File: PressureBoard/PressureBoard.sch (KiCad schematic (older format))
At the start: 9 parts, among them J1 Jack-DC, U1 MCP6002-xP, U2 L78L05_TO92

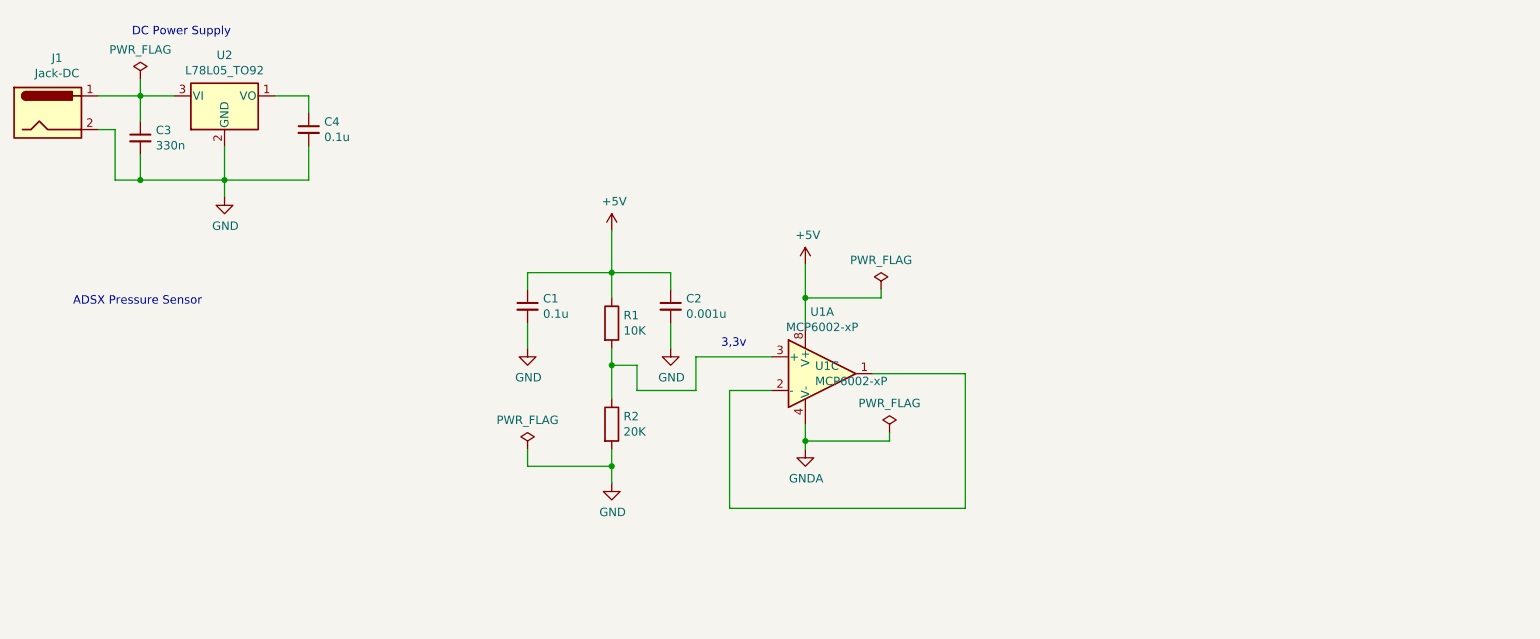
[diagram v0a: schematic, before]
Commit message: Agrego segunda versión del esquemático que incluye regulador LM7805 y sensor ASDX
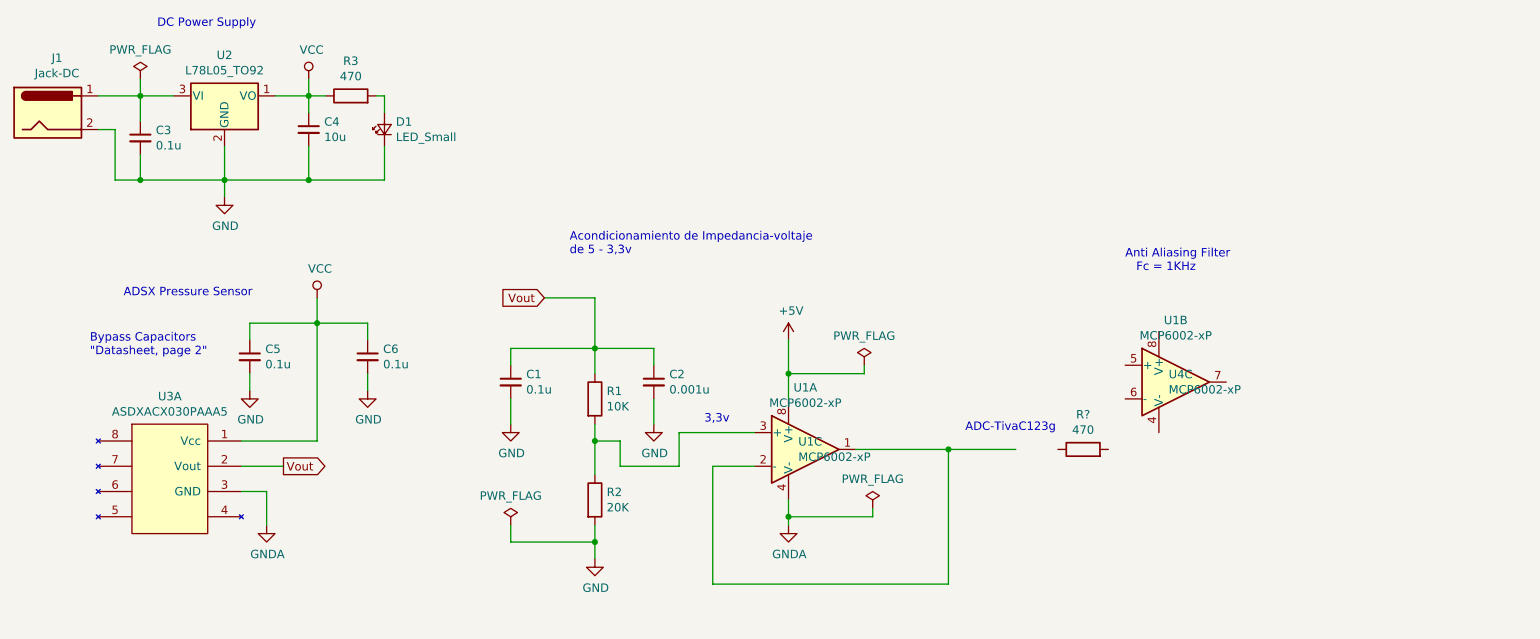
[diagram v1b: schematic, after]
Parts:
- added C5, C6: 0.1u, symbol Device:C_Small
- added D1: LED_Small, symbol Device:LED_Small
- added R3, R?: 470, symbol Device:R
- added unit 2 of U1
- added U3: ASDXACX030PAAA5, symbol ASDX:ASDXACX030PAAA5
- added U4: MCP6002-xP, symbol Amplifier_Operational:MCP6002-xP
- C3: value 330n -> 0.1u
- C4: value 0.1u -> 10u
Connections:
- net +5V: no longer C1.1, C2.1, R1.1
- net GND: now also C5.2, C6.2, D1.1 (K)
- net GNDA: now also U3.3 (GND)
- net VCC: now reaches C4.1, U2.1 (VO)
- net VCC: now also C5.1, C6.1, R3.1, U3.1 (Vcc)
- new net: D1.2 (A), R3.2
- new net Vout: C1.1, C2.1, R1.1, U3.2 (Vout)
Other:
- note added: "ADC-TivaC123g"
- note added: "Acondicionamiento de Impedancia-voltaje\nde 5 - 3,3v"
- note added: "Anti Aliasing Filter\n Fc = 1KHz"
- note added: "Bypass Capacitors\n"Datasheet, page 2""
- moved on the sheet: C1, C2, R1, R2, U1A, U1C

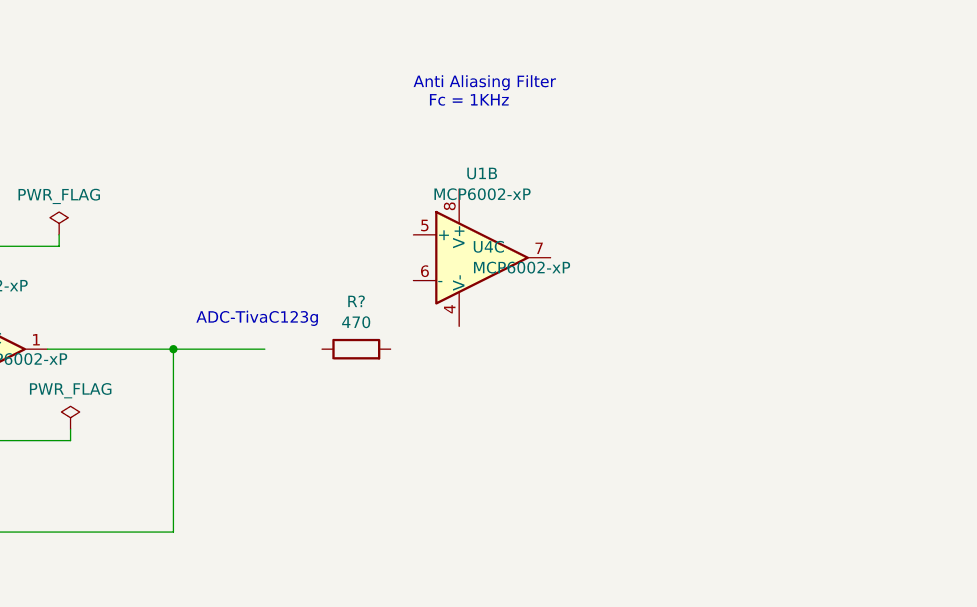
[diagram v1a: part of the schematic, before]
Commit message: Se agragan modificaciones: Filtro anti alliasing y fuente con el regulador 78L05
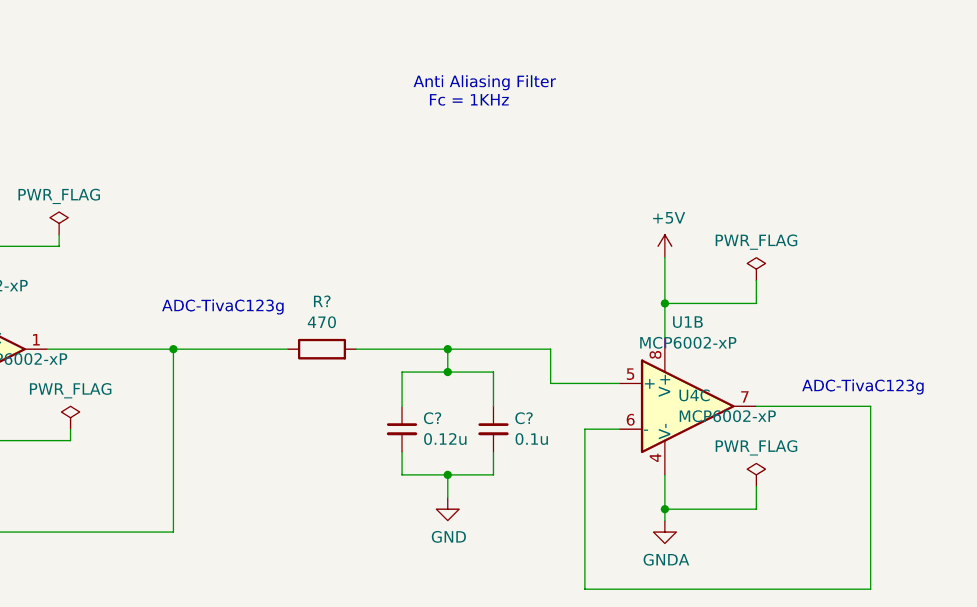
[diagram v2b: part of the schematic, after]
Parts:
- added C?: 0.1u, symbol Device:C_Small
- added C?: 0.12u, symbol Device:C_Small
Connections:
- net +5V: now also U4.8 (V+)
- net GND: now also C?.2, C?.2
- net GNDA: now also U4.4 (V-)
- net at U1.1, U1.2 (-): now also R?.1
- net at U1.5 (+): now also R?.2, C?.1, C?.1
- net at U1.6 (-): now also U1.7
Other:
- moved on the sheet: R?, U1B, U4C
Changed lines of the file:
@@
 L Amplifier_Operational:MCP6002-xP U1
 U 2 1 5C701FA7
-P 7950 2850
-F 0 "U1" H 7950 3217 50  0000 C CNN
-F 1 "MCP6002-xP" H 7950 3126 50  0000 C CNN
-F 2 "" H 7950 2850 50  0001 C CNN
-F 3 "http://ww1.microchip.com/downloads/en/DeviceDoc/21733j.pdf" H 7950 2850 50  0001 C CNN
-	2    7950 2850
+P 8850 3500
+F 0 "U1" H 8850 3867 50  0000 C CNN
+F 1 "MCP6002-xP" H 8850 3776 50  0000 C CNN
+F 2 "" H 8850 3500 50  0001 C CNN
+F 3 "http://ww1.microchip.com/downloads/en/DeviceDoc/21733j.pdf" H 8850 3500 50  0001 C CNN
+	2    8850 3500
 	1    0    0    -1
 $EndComp
@@
 L Amplifier_Operational:MCP6002-xP U4
 U 3 1 5C70202A
-P 7950 2850
-F 0 "U4" H 7908 2896 50  0000 L CNN
-F 1 "MCP6002-xP" H 7908 2805 50  0000 L CNN
-F 2 "" H 7950 2850 50  0001 C CNN
-F 3 "http://ww1.microchip.com/downloads/en/DeviceDoc/21733j.pdf" H 7950 2850 50  0001 C CNN
-	3    7950 2850
+P 8850 3500
+F 0 "U4" H 8808 3546 50  0000 L CNN
+F 1 "MCP6002-xP" H 8808 3455 50  0000 L CNN
+F 2 "" H 8850 3500 50  0001 C CNN
+F 3 "http://ww1.microchip.com/downloads/en/DeviceDoc/21733j.pdf" H 8850 3500 50  0001 C CNN
+	3    8850 3500
 	1    0    0    -1
 $EndComp
@@
 	3250 1650 3250 1450
 Connection ~ 2800 1650
-Wire Wire Line
-	6600 3250 7000 3250
 Connection ~ 6600 3250
-Text Notes 6700 3150 0    50   ~ 0
+Text Notes 6550 3100 0    50   ~ 0
 ADC-TivaC123g
 $Comp
 L Device:R R?
 U 1 1 5C71B288
-P 7400 3250
-F 0 "R?" V 7607 3250 50  0000 C CNN
-F 1 "470" V 7516 3250 50  0000 C CNN
-F 2 "" V 7330 3250 50  0001 C CNN
-F 3 "~" H 7400 3250 50  0001 C CNN
-	1    7400 3250
+P 7250 3250
+F 0 "R?" V 7457 3250 50  0000 C CNN
+F 1 "470" V 7366 3250 50  0000 C CNN
+F 2 "" V 7180 3250 50  0001 C CNN
+F 3 "~" H 7250 3250 50  0001 C CNN
+	1    7250 3250
 	0    -1   -1   0
 $EndComp
+$Comp
+L power:+5V #PWR?
+U 1 1 5C79D65E
+P 8750 2850
+F 0 "#PWR?" H 8750 2700 50  0001 C CNN
+F 1 "+5V" H 8765 3023 50  0000 C CNN
+F 2 "" H 8750 2850 50  0001 C CNN
+F 3 "" H 8750 2850 50  0001 C CNN
+	1    8750 2850
+	1    0    0    -1
+$EndComp
+$Comp
+L power:PWR_FLAG #FLG?
+U 1 1 5C79D68D
+P 9150 2950
+F 0 "#FLG?" H 9150 3025 50  0001 C CNN
+F 1 "PWR_FLAG" H 9150 3124 50  0000 C CNN
+F 2 "" H 9150 2950 50  0001 C CNN
+F 3 "~" H 9150 2950 50  0001 C CNN
+	1    9150 2950
+	1    0    0    -1
+$EndComp
+$Comp
+L power:GNDA #PWR?
+U 1 1 5C79D6BC
+P 8750 4000
+F 0 "#PWR?" H 8750 3750 50  0001 C CNN
+F 1 "GNDA" H 8755 3827 50  0000 C CNN
+F 2 "" H 8750 4000 50  0001 C CNN
+F 3 "" H 8750 4000 50  0001 C CNN
+	1    8750 4000
+	1    0    0    -1
+$EndComp
+$Comp
+L power:PWR_FLAG #FLG?
+U 1 1 5C79D6EB
+P 9150 3850
+F 0 "#FLG?" H 9150 3925 50  0001 C CNN
+F 1 "PWR_FLAG" H 9150 4024 50  0000 C CNN
+F 2 "" H 9150 3850 50  0001 C CNN
+F 3 "~" H 9150 3850 50  0001 C CNN
+	1    9150 3850
+	1    0    0    -1
+$EndComp
+Wire Wire Line
+	8750 3200 8750 3050
+Wire Wire Line
+	9150 3050 8750 3050
+Connection ~ 8750 3050
+Wire Wire Line
+	8750 3050 8750 2850
+Wire Wire Line
+	9150 3050 9150 2950
+Wire Wire Line
+	8750 3800 8750 3950
+Wire Wire Line
+	9150 3850 9150 3950
+Wire Wire Line
+	9150 3950 8750 3950
+Connection ~ 8750 3950
+Wire Wire Line
+	8750 3950 8750 4000
+$Comp
+L Device:C_Small C?
+U 1 1 5C7A4F96
+P 8000 3600
+F 0 "C?" H 8092 3646 50  0000 L CNN
+F 1 "0.1u" H 8092 3555 50  0000 L CNN
+F 2 "" H 8000 3600 50  0001 C CNN
+F 3 "~" H 8000 3600 50  0001 C CNN
+	1    8000 3600
+	1    0    0    -1
+$EndComp
+$Comp
+L power:GND #PWR?
+U 1 1 5C7A5122
+P 7800 3900
+F 0 "#PWR?" H 7800 3650 50  0001 C CNN
+F 1 "GND" H 7805 3727 50  0000 C CNN
+F 2 "" H 7800 3900 50  0001 C CNN
+F 3 "" H 7800 3900 50  0001 C CNN
+	1    7800 3900
+	1    0    0    -1
+$EndComp
+$Comp
+L Device:C_Small C?
+U 1 1 5C7A5153
+P 7600 3600
+F 0 "C?" H 7692 3646 50  0000 L CNN
+F 1 "0.12u" H 7692 3555 50  0000 L CNN
+F 2 "" H 7600 3600 50  0001 C CNN
+F 3 "~" H 7600 3600 50  0001 C CNN
+	1    7600 3600
+	1    0    0    -1
+$EndComp
+Wire Wire Line
+	6600 3250 7100 3250
+Wire Wire Line
+	8000 3700 8000 3800
+Wire Wire Line
+	8000 3800 7800 3800
+Wire Wire Line
+	7600 3800 7600 3700
+Wire Wire Line
+	7800 3900 7800 3800
+Connection ~ 7800 3800
+Wire Wire Line
+	7800 3800 7600 3800
+Wire Wire Line
+	7600 3500 7600 3350
+Wire Wire Line
+	7600 3350 7800 3350
+Wire Wire Line
+	8000 3350 8000 3500
+Wire Wire Line
+	7400 3250 7800 3250
+Wire Wire Line
+	7800 3250 7800 3350
+Connection ~ 7800 3350
+Wire Wire Line
+	7800 3350 8000 3350
+Wire Wire Line
+	7800 3250 8250 3250
+Wire Wire Line
+	8250 3250 8250 3400
+Wire Wire Line
+	8250 3400 8550 3400
+Connection ~ 7800 3250
+Wire Wire Line
+	8550 3600 8400 3600
+Wire Wire Line
+	8400 3600 8400 4300
+Wire Wire Line
+	8400 4300 9650 4300
+Wire Wire Line
+	9650 4300 9650 3500
+Wire Wire Line
+	9650 3500 9150 3500
+Text Notes 9350 3450 0    50   ~ 0
+ADC-TivaC123g
 $EndSCHEMATC
